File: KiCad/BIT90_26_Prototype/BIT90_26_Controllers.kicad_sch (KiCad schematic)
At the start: 11 parts, among them U10 74LS04, U12 74LS00, U13 74LS138, U14 74LS05, U33 74LS244, U34 74LS244, U9 74LS00

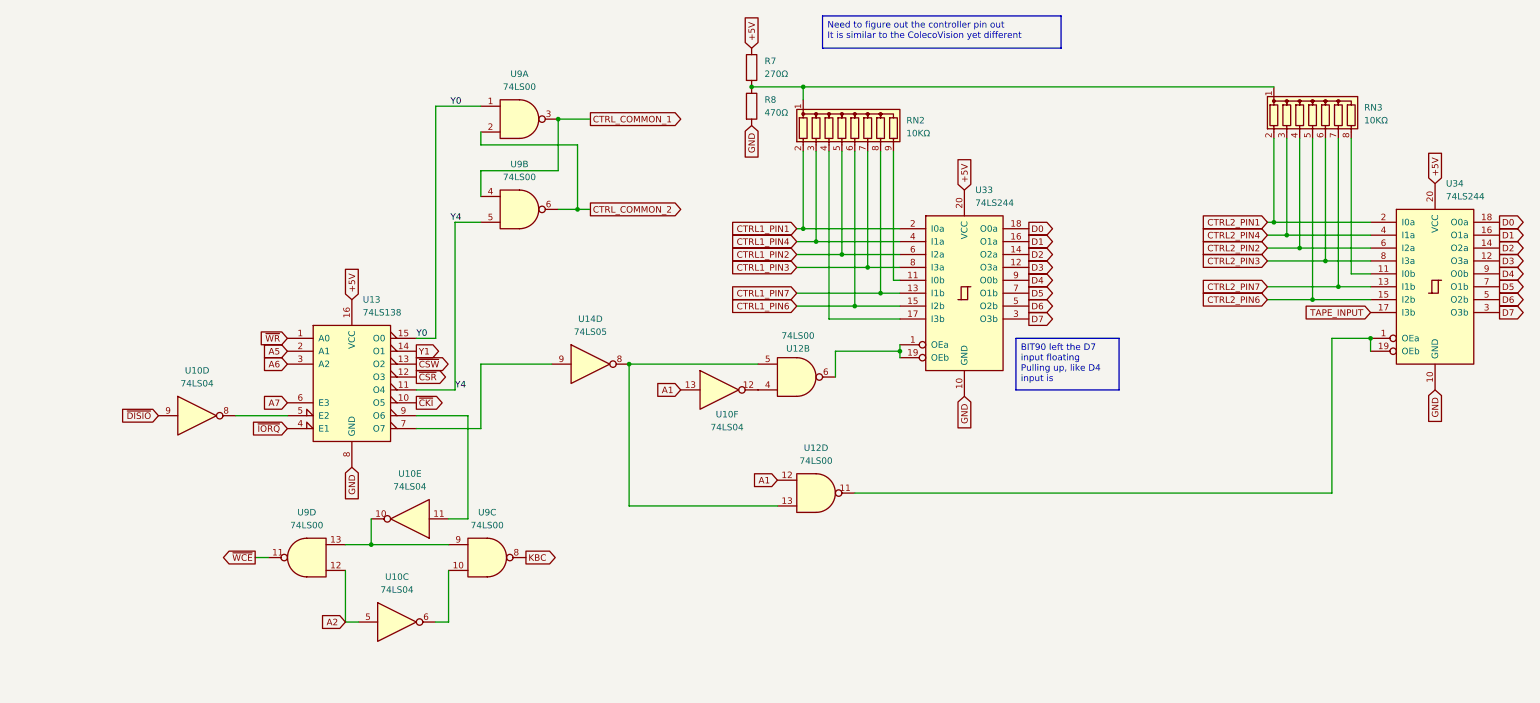
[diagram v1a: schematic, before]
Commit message: Added more signal analysis to schematic
Would be nice to reduce the amount of glue logic
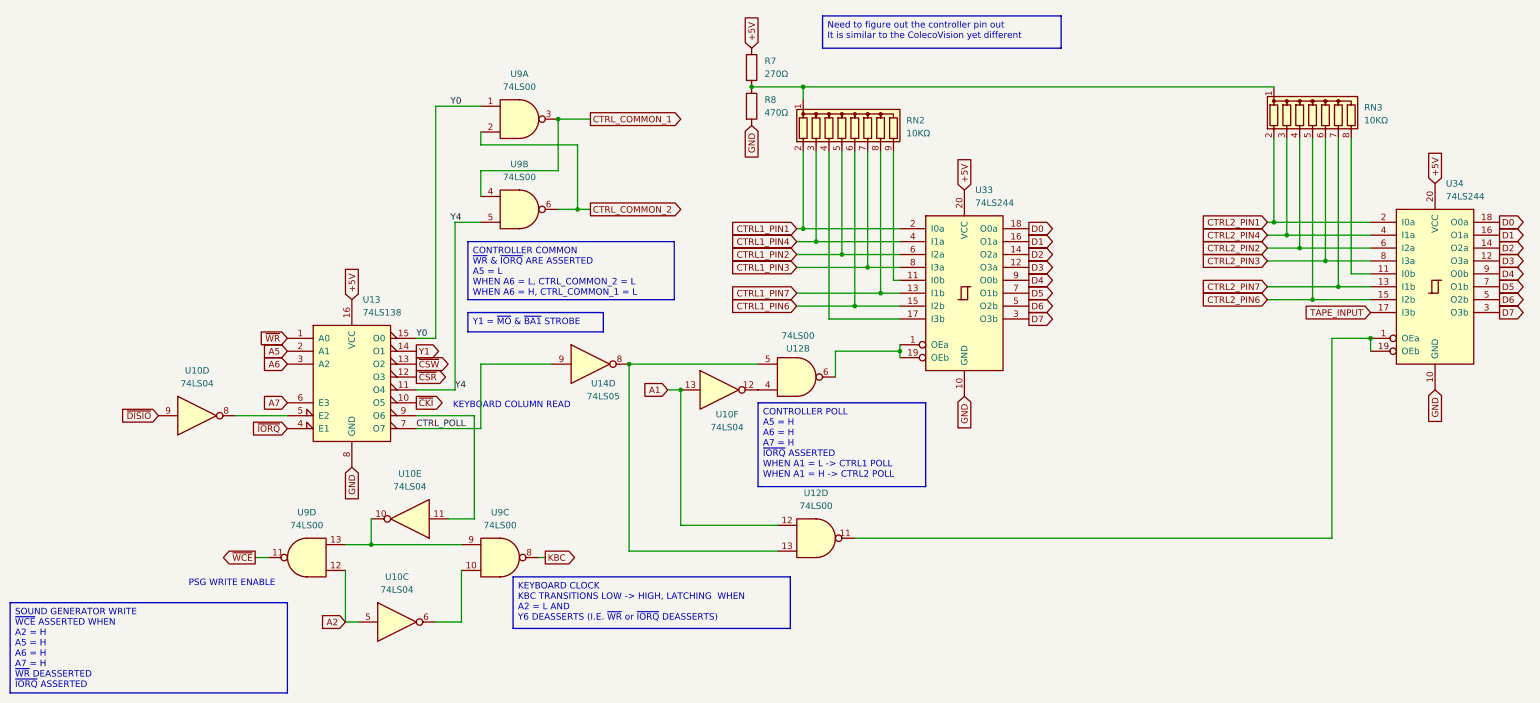
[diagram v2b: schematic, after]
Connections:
- net CTRL_POLL: now reaches U13.7 (O7), U14.9
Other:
- note added: "KEYBOARD COLUMN READ"
- note added: "PSG WRITE ENABLE"
- moved on the sheet: U12D, U9C
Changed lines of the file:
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@@
 		(comment 4 "Based on original schematics from BIT Corporation (普澤有限公司)")
 	)
+	(text "PSG WRITE ENABLE"
+		(exclude_from_sim no)
+		(at 116.078 196.85 0)
+		(effects
+			(font
+				(size 1.27 1.27)
+			)
+		)
+	)
+	(text "KEYBOARD COLUMN READ"
+		(exclude_from_sim no)
+		(at 171.196 161.798 0)
+		(effects
+			(font
+				(size 1.27 1.27)
+			)
+		)
+	)
 	(text_box "Need to figure out the controller pin out\nIt is similar to the ColecoVision yet different"
 		(exclude_from_sim no)
@@
 		)
 	)
-	(text_box "BIT90 left the D7 input floating\nPulling up, like D4 input is"
+	(text_box "KEYBOARD CLOCK\nKBC TRANSITIONS LOW -> HIGH, LATCHING  WHEN\nA2 = L AND\nY6 DEASSERTS (I.E. ~{WR} or ~{IORQ} DEASSERTS)"
+		(exclude_from_sim no)
+		(at 171.45 195.58 0)
+		(size 54.61 10.16)
+		(margins 0.9525 0.9525 0.9525 0.9525)
+		(stroke
+			(width 0)
+			(type solid)
+		)
+		(fill
+			(type none)
+		)
+		(effects
+			(font
+				(size 1.27 1.27)
+			)
+			(justify left top)
+		)
+	)
+	(text_box "CONTROLLER POLL\nA5 = H\nA6 = H\nA7 = H\n~{IORQ} ASSERTED\nWHEN A1 = L -> CTRL1 POLL\nWHEN A1 = H -> CTRL2 POLL"
 		(exclude_from_sim no)
-		(at 270.51 148.59 0)
-		(size 20.32 10.16)
+		(at 219.71 161.29 0)
+		(size 33.02 16.51)
+		(margins 0.9525 0.9525 0.9525 0.9525)
+		(stroke
+			(width 0)
+			(type solid)
+		)
+		(fill
+			(type none)
+		)
+		(effects
+			(font
+				(size 1.27 1.27)
+			)
+			(justify left top)
+		)
+	)
+	(text_box "CONTROLLER COMMON\n~{WR} & ~{IORQ} ARE ASSERTED\nA5 = L\nWHEN A6 = L, CTRL_COMMON_2 = L\nWHEN A6 = H, CTRL_COMMON_1 = L"
+		(exclude_from_sim no)
+		(at 162.56 129.54 0)
+		(size 40.64 11.43)
+		(margins 0.9525 0.9525 0.9525 0.9525)
+		(stroke
+			(width 0)
+			(type solid)
+		)
+		(fill
+			(type none)
+		)
+		(effects
+			(font
+				(size 1.27 1.27)
+			)
+			(justify left top)
+		)
+	)
+	(text_box "Y1 = ~{MO} & ~{BA1} STROBE"
+		(exclude_from_sim no)
+		(at 162.56 143.51 0)
+		(size 26.67 3.81)
+		(margins 0.9525 0.9525 0.9525 0.9525)
+		(stroke
+			(width 0)
+			(type solid)
+		)
+		(fill
+			(type none)
+		)
+		(effects
+			(font
+				(size 1.27 1.27)
+			)
+			(justify left top)
+		)
+	)
+	(text_box "SOUND GENERATOR WRITE\n~{WCE} ASSERTED WHEN\nA2 = H\nA5 = H\nA6 = H\nA7 = H\n~{WR} DEASSERTED\n~{IORQ} ASSERTED"
+		(exclude_from_sim no)
+		(at 72.39 200.66 0)
+		(size 54.61 17.78)
 		(margins 0.9525 0.9525 0.9525 0.9525)
 		(stroke
@@
 	)
 	(junction
+		(at 204.47 158.75)
+		(diameter 0)
+		(color 0 0 0 0)
+	)
+	(junction
 		(at 218.44 99.06)
 		(diameter 0)
@@
 	(wire
 		(pts
+			(xy 201.93 158.75) (xy 204.47 158.75)
+		)
+		(stroke
+			(width 0)
+			(type default)
+		)
+	)
+	(wire
+		(pts
 			(xy 228.6 127) (xy 247.65 127)
 		)
@@
 	(wire
 		(pts
-			(xy 158.75 204.47) (xy 156.21 204.47)
+			(xy 161.29 204.47) (xy 156.21 204.47)
 		)
 		(stroke
@@
 	(wire
 		(pts
-			(xy 194.31 181.61) (xy 194.31 153.67)
+			(xy 194.31 190.5) (xy 194.31 153.67)
 		)
 		(stroke
@@
 	(wire
 		(pts
-			(xy 332.74 179.07) (xy 238.76 179.07)
+			(xy 332.74 187.96) (xy 238.76 187.96)
 		)
 		(stroke
@@
 	(wire
 		(pts
-			(xy 158.75 189.23) (xy 143.51 189.23)
+			(xy 161.29 189.23) (xy 143.51 189.23)
 		)
 		(stroke
@@
 	(wire
 		(pts
+			(xy 204.47 185.42) (xy 204.47 158.75)
+		)
+		(stroke
+			(width 0)
+			(type default)
+		)
+	)
+	(wire
+		(pts
 			(xy 238.76 142.24) (xy 247.65 142.24)
 		)
@@
 	(wire
 		(pts
-			(xy 332.74 179.07) (xy 332.74 148.59)
+			(xy 332.74 187.96) (xy 332.74 148.59)
 		)
 		(stroke
@@
 	(wire
 		(pts
+			(xy 176.53 191.77) (xy 177.8 191.77)
+		)
+		(stroke
+			(width 0)
+			(type default)
+		)
+	)
+	(wire
+		(pts
 			(xy 236.22 132.08) (xy 247.65 132.08)
 		)
@@
 	(wire
 		(pts
-			(xy 162.56 184.15) (xy 162.56 163.83)
+			(xy 163.83 184.15) (xy 163.83 163.83)
 		)
 		(stroke
@@
 	(wire
 		(pts
-			(xy 162.56 163.83) (xy 152.4 163.83)
+			(xy 163.83 163.83) (xy 152.4 163.83)
 		)
 		(stroke
@@
 	(wire
 		(pts
-			(xy 223.52 181.61) (xy 194.31 181.61)
+			(xy 223.52 190.5) (xy 194.31 190.5)
 		)
 		(stroke
@@
 	(wire
 		(pts
-			(xy 158.75 184.15) (xy 162.56 184.15)
+			(xy 158.75 184.15) (xy 163.83 184.15)
 		)
 		(stroke
@@
 	(wire
 		(pts
-			(xy 158.75 194.31) (xy 158.75 204.47)
+			(xy 161.29 194.31) (xy 161.29 204.47)
 		)
 		(stroke
@@
 	(wire
 		(pts
+			(xy 223.52 185.42) (xy 204.47 185.42)
+		)
+		(stroke
+			(width 0)
+			(type default)
+		)
+	)
+	(wire
+		(pts
 			(xy 331.47 109.22) (xy 331.47 133.35)
 		)
@@
 		)
 	)
+	(label "CTRL_POLL"
+		(at 152.4 166.37 0)
+		(effects
+			(font
+				(size 1.27 1.27)
+			)
+			(justify left bottom)
+		)
+	)
 	(label "Y0"
 		(at 161.29 102.87 180)
@@
 	(global_label "KBC"
 		(shape output)
-		(at 173.99 191.77 0)
+		(at 177.8 191.77 0)
 		(fields_autoplaced yes)
 		(effects
@@
 		)
 		(property "Intersheetrefs" "${INTERSHEET_REFS}"
-			(at 180.7852 191.77 0)
+			(at 184.5952 191.77 0)
 			(effects
 				(font
@@
 		)
 	)
-	(global_label "A1"
-		(shape input)
-		(at 223.52 176.53 180)
-		(fields_autoplaced yes)
-		(effects
-			(font
-				(size 1.27 1.27)
-			)
-			(justify right)
-		)
-		(property "Intersheetrefs" "${INTERSHEET_REFS}"
-			(at 218.2367 176.53 0)
-			(effects
-				(font
-					(size 1.27 1.27)
-				)
-				(justify right)
-				(hide yes)
-			)
-		)
-	)
 	(global_label "~{CSR}"
 		(shape output)
@@
 	(global_label "A1"
 		(shape input)
-		(at 204.47 158.75 180)
+		(at 201.93 158.75 180)
 		(fields_autoplaced yes)
 		(effects
@@
 		)
 		(property "Intersheetrefs" "${INTERSHEET_REFS}"
-			(at 199.1867 158.75 0)
+			(at 196.6467 158.75 0)
 			(effects
 				(font
@@
 		(on_board yes)
 		(dnp no)
-		(fields_autoplaced yes)
 		(property "Reference" "U14"
-			(at 186.69 144.78 0)
+			(at 189.23 157.48 0)
 			(effects
 				(font
@@
 		)
 		(property "Value" "74LS05"
-			(at 186.69 147.32 0)
+			(at 189.23 160.02 0)
 			(effects
 				(font
@@
 	(symbol
 		(lib_id "74xx:74LS00")
-		(at 166.37 191.77 0)
+		(at 168.91 191.77 0)
 		(unit 3)
 		(exclude_from_sim no)
@@
 		(fields_autoplaced yes)
 		(property "Reference" "U9"
-			(at 166.3617 182.88 0)
+			(at 168.9017 182.88 0)
 			(effects
 				(font
@@
 		)
 		(property "Value" "74LS00"
-			(at 166.3617 185.42 0)
+			(at 168.9017 185.42 0)
 			(effects
 				(font
@@
 		)
 		(property "Footprint" "Package_DIP:DIP-14_W7.62mm"
-			(at 166.37 191.77 0)
+			(at 168.91 191.77 0)
 			(effects
 				(font
@@
 		)
 		(property "Datasheet" "http://www.ti.com/lit/gpn/sn74ls00"
-			(at 166.37 191.77 0)
+			(at 168.91 191.77 0)
 			(effects
 				(font
@@
 		)
 		(property "Description" "quad 2-input NAND gate"
-			(at 166.37 191.77 0)
+			(at 168.91 191.77 0)
 			(effects
 				(font
@@
 	(symbol
 		(lib_id "74xx:74LS00")
-		(at 231.14 179.07 0)
+		(at 231.14 187.96 0)
 		(unit 4)
 		(exclude_from_sim no)
@@
 		(fields_autoplaced yes)
 		(property "Reference" "U12"
-			(at 231.1317 170.18 0)
+			(at 231.1317 179.07 0)
 			(effects
 				(font
@@
 		)
 		(property "Value" "74LS00"
-			(at 231.1317 172.72 0)
+			(at 231.1317 181.61 0)
 			(effects
 				(font
@@
 		)
 		(property "Footprint" "Package_DIP:DIP-14_W7.62mm"
-			(at 231.14 179.07 0)
+			(at 231.14 187.96 0)
 			(effects
 				(font
@@
 		)
 		(property "Datasheet" "http://www.ti.com/lit/gpn/sn74ls00"
-			(at 231.14 179.07 0)
+			(at 231.14 187.96 0)
 			(effects
 				(font
@@
 		)
 		(property "Description" "quad 2-input NAND gate"
-			(at 231.14 179.07 0)
+			(at 231.14 187.96 0)
 			(effects
 				(font
